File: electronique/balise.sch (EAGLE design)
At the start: 46 parts

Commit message: maj elec balise
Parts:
- added LED1, LED13, LED14, LED15, LED16, LED17, LED18, LED19, LED2, LED3: orange, led:LED5MM
- added LED10, LED11, LED12: bleu, led:LED5MM
- added LED4, LED5, LED6: jaune, led:LED5MM
- added LED7, LED8, LED9: vert, led:LED5MM
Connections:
- removed net DEL_CH_1: R10.2, R12.2, R14.2, R16.2, R18.2, R2.2, R20.2, R22.2, R24.2, R6.2, R8.2
- removed net DEL_CH_2: R4.2
- removed net DEL_CTRL_1: R1.2, R11.2, R13.2, R15.2, R17.2, R19.2, R21.2, R23.2, R7.2, R9.2
- removed net DEL_CTRL_2: R3.2
- removed net DEL_CTRL_3: R5.2
- removed net N$28: RPI.GPIO17/GEN0
- removed net N$29: RPI.GPIO27/GEN2
- removed net N$30: RPI.GPIO22/GEN3
- removed net N$31: RPI.GPIO5
- removed net N$32: RPI.GPIO6
- removed net N$33: RPI.GPIO13
- removed net N$34: RPI.GPIO19
- removed net N$35: RPI.GPIO26
- removed net N$36: RPI.GPIO10/MOSI
- removed net N$37: RPI.GPIO9/MISO
- removed net N$38: RPI.GPIO11/SCLK
- new net DEL_BLEU_1: LED10.A, R20.2
- new net DEL_BLEU_1_PWM: R19.2, RPI.GPIO19
- new net DEL_BLEU_2: LED11.A, R22.2
- new net DEL_BLEU_2_PWM: R21.2, RPI.GPIO26
- new net DEL_BLEU_3: LED12.A, R24.2
- new net DEL_BLEU_3_PWM: R23.2, RPI.GPIO21
- new net DEL_JAUNE_1: LED4.A, LED5.A, LED6.A, R14.2
- new net DEL_JAUNE_1_PWM: R13.2, RPI.GPIO10/MOSI
- new net DEL_JAUNE_2: R16.2
- new net DEL_JAUNE_2_PWM: R15.2, RPI.GPIO9/MISO
- new net DEL_JAUNE_3: R18.2
- new net DEL_JAUNE_3_PWM: R17.2, RPI.GPIO11/SCLK
- new net DEL_ORANGE_1: LED1.A, R2.2
- new net DEL_ORANGE_1_PWM: R1.2, RPI.GPIO17/GEN0
- new net DEL_ORANGE_2: LED2.A, R4.2
- new net DEL_ORANGE_2_PWM: R3.2, RPI.GPIO27/GEN2
- new net DEL_ORANGE_3: LED3.A, R6.2
- new net DEL_ORANGE_3_PWM: R5.2, RPI.GPIO22/GEN3
- new net DEL_VERT_1: LED7.A, R8.2
- new net DEL_VERT_1_PWM: R7.2, RPI.GPIO5
- new net DEL_VERT_2: LED8.A, R10.2
- new net DEL_VERT_2_PWM: R9.2, RPI.GPIO6
- new net DEL_VERT_3: LED9.A, R12.2
- new net DEL_VERT_3_PWM: R11.2, RPI.GPIO13
- net GND: now also LED1.C, LED10.C, LED11.C, LED12.C, LED2.C, LED3.C, LED4.C, LED5.C, LED6.C, LED7.C, LED8.C, LED9.C
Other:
- moved on the sheet: R13, R14, R15, R16, R17, R18, R19, R20, R21, R22, R23, R24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

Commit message: Ajout élec balise
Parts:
- removed LED1, LED13, LED14, LED15, LED16, LED17, LED18, LED19, LED2, LED3: orange, led:LED5MM
- removed LED10, LED11, LED12: bleu, led:LED5MM
- removed LED4, LED5, LED6: jaune, led:LED5MM
- removed LED7, LED8, LED9: vert, led:LED5MM
- removed R10, R12, R2, R4, R6, R8: 0, resistor:R-EU_R0805
- removed R11, R3, R5, R7, R9: 270, resistor:R-EU_R0805
- removed T1, T10, T11, T12, T2, T3, T4, T9: (no value), transistor:BC817-16-NPN-SOT23-BEC
- added C3: 10µF, resistor:C-EUC0805
- added LED100, LED117, LED118, LED119, LED120, LED121, LED122, LED123, LED132, LED149, LED150, LED151, LED152, LED153, LED154, LED155, LED34, LED51, LED52, LED53, LED54, LED55, LED56, LED57: jaune, led:LED5MM
- added LED101, LED110, LED111, LED112, LED113, LED114, LED115, LED116, LED133, LED142, LED143, LED144, LED145, LED146, LED147, LED148, LED35, LED44, LED45, LED46, LED47, LED48, LED49, LED50, LED97: vert, led:LED5MM
- added LED102, LED124, LED125, LED126, LED127, LED128, LED129, LED130, LED134, LED156, LED157, LED158, LED159, LED160, LED161, LED162, LED36, LED58, LED59, LED60, LED61, LED62, LED63, LED64, LED98: bleu, led:LED5MM
- added LED103, LED104, LED105, LED106, LED107, LED108, LED109, LED131, LED135, LED136, LED137, LED138, LED139, LED140, LED141, LED33, LED37, LED38, LED39, LED40, LED41, LED42, LED43, LED99: orange, led:LED5MM
- added R37: 1k, resistor:R-EU_R0805
- added R38: 470, resistor:R-EU_R0805
- added R39, R40, R41, R42, R43, R44, R45, R46, R51, R52, R53, R54, R55, R56, R57, R58: 0, resistor:R-EU_R0805
- added R47, R48, R49, R50, R59, R60, R61, R62: 270, resistor:R-EU_R0805
- added T13, T14, T15, T16, T17, T18, T19, T20: (no value), transistor:BC817-16-NPN-SOT23-BEC
- added U$1: PUSH-BUTTON, push-button:PUSH-BUTTON
- R1: value 270 -> 1k
- R13, R15, R17, R19: value 270 -> 0
- R22, R24: value 0 -> 270
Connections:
- removed net +3V3: DC2.VOUT, T1.C, T10.C, T11.C, T12.C, T2.C, T3.C, T4.C, T5.C, T6.C, T7.C, T8.C, T9.C
- removed net N$10: R7.1, T4.B
- removed net N$16: R13.1, T7.B
- removed net N$17: R14.1, T7.E
- removed net N$19: R16.1, T8.E
- removed net N$22: R19.1, T10.B
- removed net N$24: R21.1, T11.B
- removed net N$25: R22.1, T11.E
- removed net N$26: R23.1, T12.B
- removed net N$27: R24.1, T12.E
- removed net N$3: R1.1, T1.B
- removed net N$5: R2.1, T1.E
- removed net N$7: R4.1, T2.E
- new net 3V3@1: R1.1, RPI.3V3@1
- new net DEL_POWER: DC2.VOUT, T13.C, T14.C, T15.C, T16.C, T17.C, T18.C, T19.C, T20.C, T5.C, T6.C, T7.C, T8.C
- new net N$40: LED97.A, R37.2
- new net N$41: R38.1, RPI.GPIO20
- new net N$42: LED98.A, R38.2
- new net N$43: LED103.C, LED104.C, LED105.C, LED99.C, R39.1
- new net N$44: LED106.C, LED107.C, LED108.C, LED109.C, R40.1
- new net N$45: LED101.C, LED110.C, LED111.C, LED112.C, R41.1
- new net N$46: LED113.C, LED114.C, LED115.C, LED116.C, R42.1
- new net N$47: LED100.C, LED117.C, LED118.C, LED119.C, R43.1
- new net N$48: LED120.C, LED121.C, LED122.C, LED123.C, R44.1
- new net N$49: LED102.C, LED124.C, LED125.C, LED126.C, R45.1
- new net N$50: LED127.C, LED128.C, LED129.C, LED130.C, R46.1
- new net N$51: R47.1, T13.B
- new net N$52: R48.1, T14.B
- new net N$53: R49.1, T15.B
- new net N$54: R50.1, T16.B
- new net N$55: LED131.C, LED135.C, LED136.C, LED137.C, R51.1
- new net N$56: LED138.C, LED139.C, LED140.C, LED141.C, R52.1
- new net N$57: LED133.C, LED142.C, LED143.C, LED144.C, R53.1
- new net N$58: LED145.C, LED146.C, LED147.C, LED148.C, R54.1
- new net N$59: LED132.C, LED149.C, LED150.C, LED151.C, R55.1
- new net N$60: LED152.C, LED153.C, LED154.C, LED155.C, R56.1
- new net N$61: LED134.C, LED156.C, LED157.C, LED158.C, R57.1
- new net N$62: LED159.C, LED160.C, LED161.C, LED162.C, R58.1
- new net N$63: R59.1, T17.B
- new net N$64: R60.1, T18.B
- new net N$65: R61.1, T19.B
- new net N$66: R62.1, T20.B
- new net POWEROFF: C3.2, R1.2, RPI.GPIO16, U$1.P$1
- net +5V: now also R37.1
- net DEL_BLEU_1: now also LED134.A, LED156.A, LED157.A, LED158.A, LED159.A, LED160.A, LED161.A, LED162.A, T20.E; no longer LED10.A, R20.2
- net DEL_BLEU_1_PWM: now also R62.2; no longer R19.2
- net DEL_BLEU_2: now also LED36.A, LED58.A, LED59.A, LED60.A, LED61.A, LED62.A, LED63.A, LED64.A, T8.E; no longer LED11.A, R22.2
- net DEL_BLEU_2_PWM: now also R24.2; no longer R21.2
- net DEL_BLEU_3: now also LED102.A, LED124.A, LED125.A, LED126.A, LED127.A, LED128.A, LED129.A, LED130.A, T16.E; no longer LED12.A, R24.2
- net DEL_BLEU_3_PWM: now also R50.2; no longer R23.2
- net DEL_JAUNE_1: now also LED132.A, LED149.A, LED150.A, LED151.A, LED152.A, LED153.A, LED154.A, LED155.A, T19.E; no longer LED4.A, LED5.A, LED6.A, R14.2
- net DEL_JAUNE_1_PWM: now also R61.2; no longer R13.2
- net DEL_JAUNE_2: now also LED34.A, LED51.A, LED52.A, LED53.A, LED54.A, LED55.A, LED56.A, LED57.A, T7.E; no longer R16.2
- net DEL_JAUNE_2_PWM: now also R23.2; no longer R15.2
- net DEL_JAUNE_3: now also LED100.A, LED117.A, LED118.A, LED119.A, LED120.A, LED121.A, LED122.A, LED123.A, T15.E; no longer R18.2
- net DEL_JAUNE_3_PWM: now also R49.2; no longer R17.2
- net DEL_ORANGE_1: now also LED131.A, LED135.A, LED136.A, LED137.A, LED138.A, LED139.A, LED140.A, LED141.A, T17.E; no longer LED1.A, R2.2
- net DEL_ORANGE_1_PWM: now also R59.2; no longer R1.2
- net DEL_ORANGE_2: now also LED33.A, LED37.A, LED38.A, LED39.A, LED40.A, LED41.A, LED42.A, LED43.A, T5.E; no longer LED2.A, R4.2
- net DEL_ORANGE_2_PWM: now also R21.2; no longer R3.2
- net DEL_ORANGE_3: now also LED103.A, LED104.A, LED105.A, LED106.A, LED107.A, LED108.A, LED109.A, LED99.A, T13.E; no longer LED3.A, R6.2
- net DEL_ORANGE_3_PWM: now also R47.2; no longer R5.2
- net DEL_VERT_1: now also LED133.A, LED142.A, LED143.A, LED144.A, LED145.A, LED146.A, LED147.A, LED148.A, T18.E; no longer LED7.A, R8.2
- net DEL_VERT_1_PWM: now also R60.2; no longer R7.2
- net DEL_VERT_2: now also LED35.A, LED44.A, LED45.A, LED46.A, LED47.A, LED48.A, LED49.A, LED50.A, T6.E; no longer LED8.A, R10.2
- net DEL_VERT_2_PWM: now also R22.2; no longer R9.2
- net DEL_VERT_3: now also LED101.A, LED110.A, LED111.A, LED112.A, LED113.A, LED114.A, LED115.A, LED116.A, T14.E; no longer LED9.A, R12.2
- net DEL_VERT_3_PWM: now also R48.2; no longer R11.2
- net GND: now also C3.1, LED97.C, LED98.C, R13.2, R14.2, R15.2, R16.2, R17.2, R18.2, R19.2, R20.2, R39.2, R40.2, R41.2, R42.2, R43.2, R44.2, R45.2, R46.2, R51.2, R52.2, R53.2, R54.2, R55.2, R56.2, R57.2, R58.2, U$1.P$2; no longer LED1.C, LED10.C, LED11.C, LED12.C, LED2.C, LED3.C, LED4.C, LED5.C, LED6.C, LED7.C, LED8.C, LED9.C
- net N$11: now also LED47.C, LED48.C, LED49.C, LED50.C, R16.1; no longer R8.1, T4.E
- net N$12: now also LED34.C, LED51.C, LED52.C, LED53.C, R17.1; no longer R9.1, T5.B
- net N$13: now also LED54.C, LED55.C, LED56.C, LED57.C, R18.1; no longer R10.1, T5.E
- net N$14: now also LED36.C, LED58.C, LED59.C, LED60.C, R19.1; no longer R11.1, T6.B
- net N$15: now also LED61.C, LED62.C, LED63.C, LED64.C, R20.1; no longer R12.1, T6.E
- net N$18: now also R21.1, T5.B; no longer R15.1, T8.B
- net N$20: now also R22.1, T6.B; no longer R17.1, T9.B
- net N$21: now also R23.1, T7.B; no longer R18.1, T9.E
- net N$23: now also R24.1, T8.B; no longer R20.1, T10.E
- net N$6: now also LED33.C, LED37.C, LED38.C, LED39.C, R13.1; no longer R3.1, T2.B
- net N$8: now also LED40.C, LED41.C, LED42.C, LED43.C, R14.1; no longer R5.1, T3.B
- net N$9: now also LED35.C, LED44.C, LED45.C, LED46.C, R15.1; no longer R6.1, T3.E
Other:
- moved on the sheet: R1, R13, R14, R15, R16, R17, R18, R19, R20, R21, R22, R23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

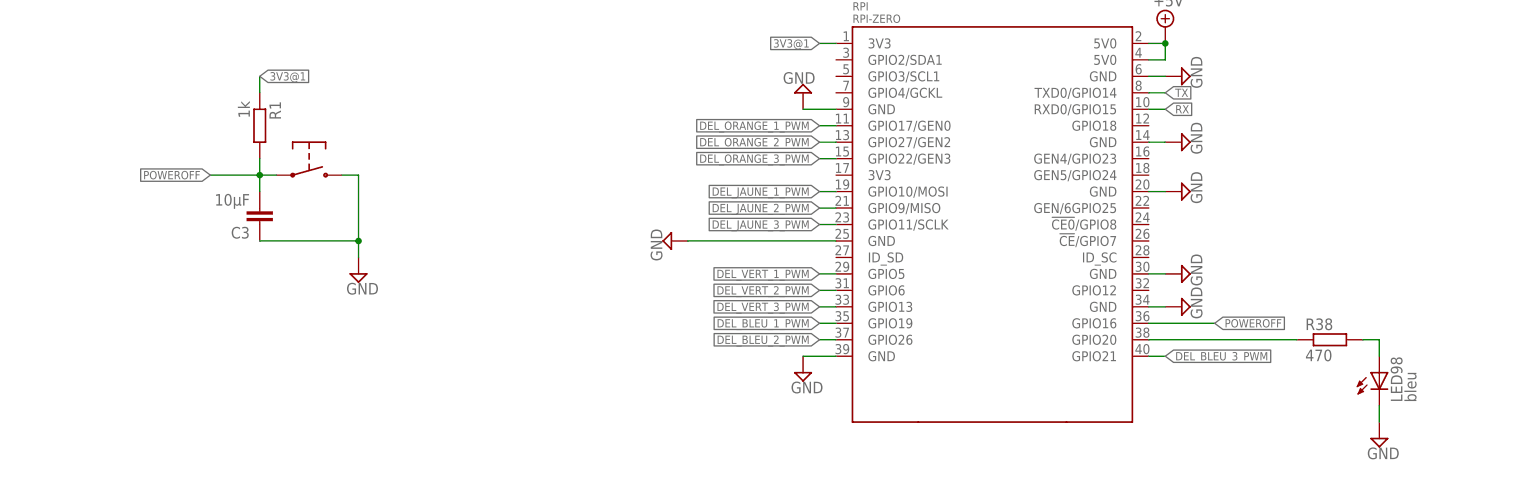
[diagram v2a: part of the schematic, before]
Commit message: Elec balise routée !
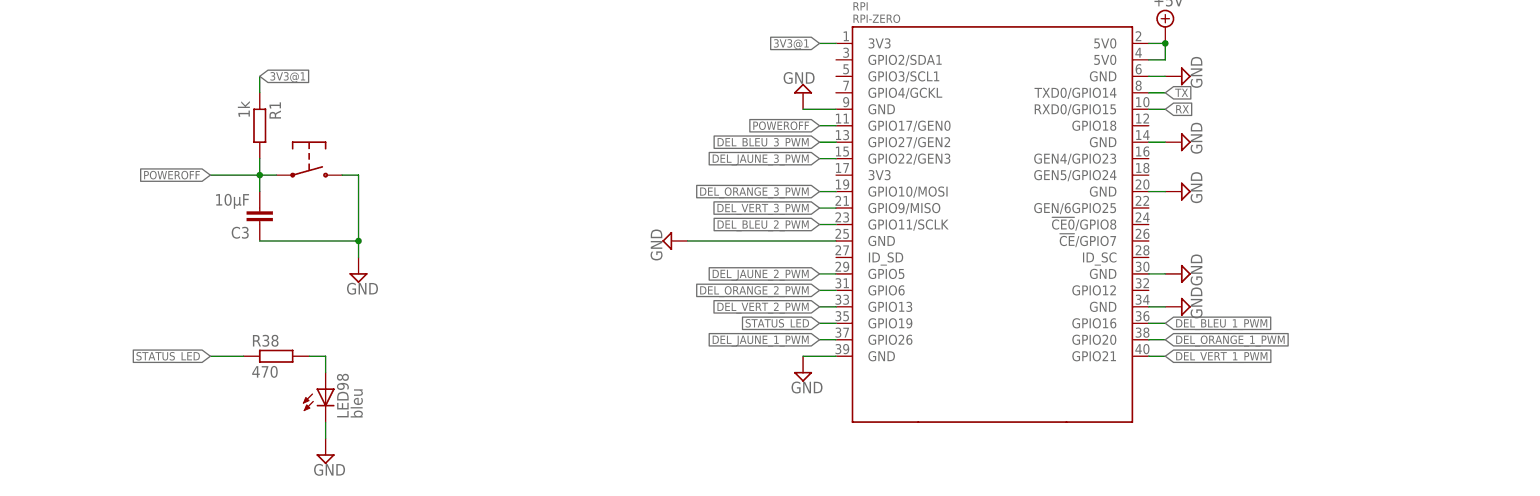
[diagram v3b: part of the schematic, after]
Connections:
- removed net N$41: R38.1, RPI.GPIO20
- new net STATUS_LED: R38.1, RPI.GPIO19
- net DEL_BLEU_1_PWM: now also RPI.GPIO16; no longer RPI.GPIO19
- net DEL_BLEU_2_PWM: now also RPI.GPIO11/SCLK; no longer RPI.GPIO26
- net DEL_BLEU_3_PWM: now also RPI.GPIO27/GEN2; no longer RPI.GPIO21
- net DEL_JAUNE_1_PWM: now also RPI.GPIO26; no longer RPI.GPIO10/MOSI
- net DEL_JAUNE_2_PWM: now also RPI.GPIO5; no longer RPI.GPIO9/MISO
- net DEL_JAUNE_3_PWM: now also RPI.GPIO22/GEN3; no longer RPI.GPIO11/SCLK
- net DEL_ORANGE_1_PWM: now also RPI.GPIO20; no longer RPI.GPIO17/GEN0
- net DEL_ORANGE_2_PWM: now also RPI.GPIO6; no longer RPI.GPIO27/GEN2
- net DEL_ORANGE_3_PWM: now also RPI.GPIO10/MOSI; no longer RPI.GPIO22/GEN3
- net DEL_VERT_1_PWM: now also RPI.GPIO21; no longer RPI.GPIO5
- net DEL_VERT_2_PWM: now also RPI.GPIO13; no longer RPI.GPIO6
- net DEL_VERT_3_PWM: now also RPI.GPIO9/MISO; no longer RPI.GPIO13
- net POWEROFF: now also RPI.GPIO17/GEN0; no longer RPI.GPIO16
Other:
- moved on the sheet: LED98, R38

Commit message: Elec version finale + Ajout fichiers gerber
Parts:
- S1: RS (none) -> 913-9069
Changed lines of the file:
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@@
 <part name="SUPPLY13" library="supply2" library_urn="urn:adsk.eagle:library:372" deviceset="GND" device=""/>
 <part name="SUPPLY14" library="supply2" library_urn="urn:adsk.eagle:library:372" deviceset="GND" device=""/>
-<part name="S1" library="switch" library_urn="urn:adsk.eagle:library:380" deviceset="TL36PO" device="" package3d_urn="urn:adsk.eagle:package:27745/1"/>
+<part name="S1" library="switch" library_urn="urn:adsk.eagle:library:380" deviceset="TL36PO" device="" package3d_urn="urn:adsk.eagle:package:27745/1">
+<attribute name="RS" value="913-9069"/>
+</part>
 <part name="SUPPLY15" library="supply2" library_urn="urn:adsk.eagle:library:372" deviceset="+12V" device=""/>
 <part name="DC2" library="dc-dc-converter" library_urn="urn:adsk.eagle:library:208" deviceset="R-78C*-1.0" device="" package3d_urn="urn:adsk.eagle:package:12318/1" technology="3.3"/>
@@
 <instance part="SUPPLY13" gate="GND" x="149.86" y="154.94" rot="R270"/>
 <instance part="SUPPLY14" gate="GND" x="200.66" y="144.78"/>
-<instance part="S1" gate="BEF1" x="233.68" y="154.94" rot="R270"/>
+<instance part="S1" gate="BEF1" x="233.68" y="154.94" rot="R270">
+<attribute name="RS" x="233.68" y="154.94" size="1.778" layer="96" rot="R270" display="off"/>
+</instance>
 <instance part="SUPPLY15" gate="+12V" x="243.84" y="160.02"/>
 <instance part="DC2" gate="G$1" x="99.06" y="152.4"/>
